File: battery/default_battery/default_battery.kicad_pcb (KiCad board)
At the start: 2 copper layers, 14 parts

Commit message: add battery_led_back
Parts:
- moved BAT_Q1 0.65 mm to (0.00, -41.3)
- moved BAT_AP1 0.37 mm to (0.00, -37.4), turned to -90 degrees
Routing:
- net VBUS: track 28.5 -> 24.9 mm, vias 1 -> 0
- net GND: track 37.8 -> 38.9 mm
- net Net-(BAT_AP1-EN): track 11.0 -> 10.5 mm

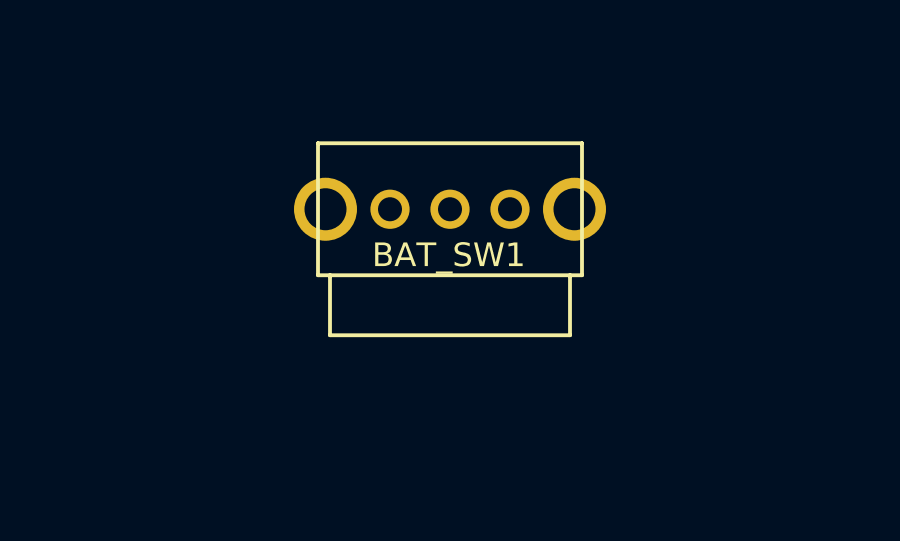
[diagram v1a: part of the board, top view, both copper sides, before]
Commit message: update battery switch symbol
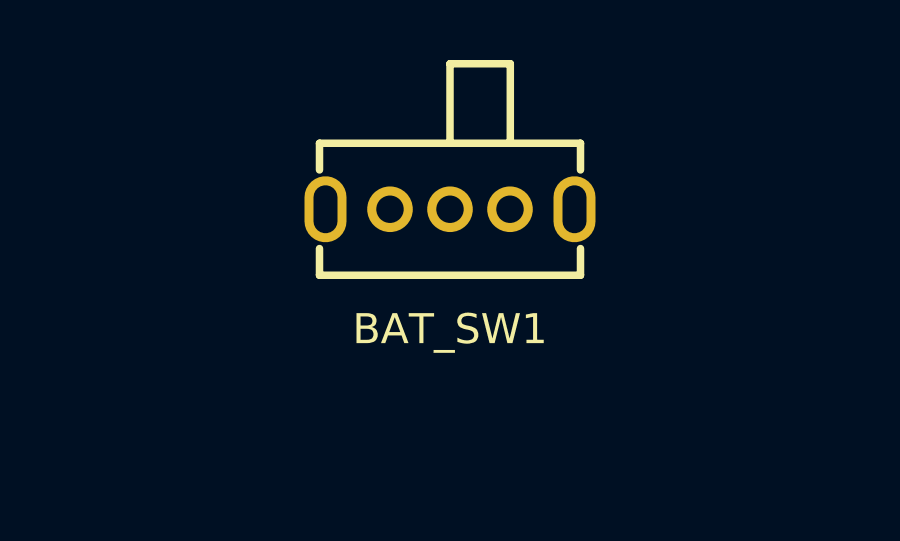
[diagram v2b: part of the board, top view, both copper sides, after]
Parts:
- BAT_SW1: footprint ErgoCai.pretty:SK12D07VG4 -> easyeda2kicad:SW-TH_SK12D07VG4
- turned BAT_SW1 to 180 degrees
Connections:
- BAT_SW1 pad 2: unconnected-(BAT_SW1-Pad2) -> VBAT
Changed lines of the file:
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@@
 	(net 12 "Net-(BAT_TP1-~{CHRG})")
 	(net 13 "Net-(BAT_TP1-PROG)")
-	(net 14 "unconnected-(BAT_SW1-Pad2)")
+	(net 14 "unconnected-(BAT_SW1-Pad3)")
 	(footprint "ErgoCai.pretty:R_0603_1608Metric"
 		(layer "F.Cu")
@@
 			)
 		)
-		(property "Datasheet" ""
+		(property "Datasheet" "~"
 			(at 0 0 0)
 			(unlocked yes)
@@
 			)
 		)
-		(property "Datasheet" ""
+		(property "Datasheet" "~"
 			(at 0 0 180)
 			(unlocked yes)
@@
 			)
 		)
-		(property "Datasheet" ""
+		(property "Datasheet" "~"
 			(at 0 0 180)
 			(unlocked yes)
@@
 			)
 		)
-		(property "Datasheet" ""
+		(property "Datasheet" "~"
 			(at 0 0 180)
 			(unlocked yes)
@@
 			)
 		)
-		(property "Datasheet" ""
+		(property "Datasheet" "~"
 			(at 0 0 180)
 			(unlocked yes)
@@
 			)
 		)
-		(property "Datasheet" ""
+		(property "Datasheet" "~"
 			(at 0 0 180)
 			(unlocked yes)
@@
 			)
 		)
-		(property "Datasheet" ""
+		(property "Datasheet" "~"
 			(at 0 0 0)
 			(unlocked yes)
@@
 		)
 	)
-	(footprint "ErgoCai.pretty:SK12D07VG4"
+	(footprint "easyeda2kicad:SW-TH_SK12D07VG4"
 		(layer "F.Cu")
-		(at -0.49 -58.65)
+		(at -0.49 -58.65 180)
 		(property "Reference" "BAT_SW1"
-			(at -0.04 1.53 0)
-			(layer "F.SilkS")
-			(effects
-				(font
-					(size 0.787402 0.787402)
+			(at 0 -4 0)
+			(layer "F.SilkS")
+			(effects
+				(font
+					(size 1 1)
 					(thickness 0.15)
 				)
@@
 		)
 		(property "Value" "~"
-			(at 0.01 3.18 0)
-			(layer "F.Fab")
-			(effects
-				(font
-					(size 0.787402 0.787402)
-					(thickness 0.15)
-				)
-			)
-		)
-		(property "Datasheet" ""
+			(at 0 4 0)
+			(layer "F.Fab")
+			(effects
+				(font
+					(size 1 1)
+					(thickness 0.15)
+				)
+			)
+		)
+		(property "Datasheet" "https://lcsc.com/product-detail/Toggle-Switches_SHOU-HAN-SK12D07VG4_C393937.html"
 			(at 0 0 0)
 			(layer "F.Fab")
@@
 		)
 		(property "MF" "C&K"
-			(at 0 0 0)
+			(at 0 0 180)
 			(unlocked yes)
 			(layer "F.Fab")
@@
 		)
 		(property "Description_1" "Switch Slide ON ON SPDT Side Slide 0.3A 30VDC PC Pins Bracket Mount/Through Hole Bulk"
-			(at 0 0 0)
+			(at 0 0 180)
 			(unlocked yes)
 			(layer "F.Fab")
@@
 		)
 		(property "Package" "None"
-			(at 0 0 0)
+			(at 0 0 180)
 			(unlocked yes)
 			(layer "F.Fab")
@@
 		)
 		(property "Price" "None"
-			(at 0 0 0)
+			(at 0 0 180)
 			(unlocked yes)
 			(layer "F.Fab")
@@
 		)
 		(property "SnapEDA_Link" "https://www.snapeda.com/parts/SK12D07VG4/C%2526K/view-part/?ref=snap"
-			(at 0 0 0)
+			(at 0 0 180)
 			(unlocked yes)
 			(layer "F.Fab")
@@
 		)
 		(property "MP" "SK12D07VG4"
-			(at 0 0 0)
+			(at 0 0 180)
 			(unlocked yes)
 			(layer "F.Fab")
@@
 		)
 		(property "Availability" "Not in stock"
-			(at 0 0 0)
+			(at 0 0 180)
 			(unlocked yes)
 			(layer "F.Fab")
@@
 		)
 		(property "Check_prices" "https://www.snapeda.com/parts/SK12D07VG4/C%2526K/view-part/?ref=eda"
-			(at 0 0 0)
+			(at 0 0 180)
+			(unlocked yes)
+			(layer "F.Fab")
+			(hide yes)
+			(effects
+				(font
+					(size 1 1)
+					(thickness 0.15)
+				)
+			)
+		)
+		(property "LCSC Part" "C393937"
+			(at 0 0 180)
 			(unlocked yes)
 			(layer "F.Fab")
@@
 		(attr through_hole)
 		(fp_line
-			(start -4.4 -2.2)
-			(end 4.4 -2.2)
-			(stroke
-				(width 0.127)
-				(type solid)
-			)
-			(layer "F.SilkS")
-		)
-		(fp_line
-			(start -4.4 2.2)
-			(end -4.4 -2.2)
-			(stroke
-				(width 0.127)
-				(type solid)
-			)
-			(layer "F.SilkS")
-		)
-		(fp_line
-			(start -4 2.2)
-			(end -4.4 2.2)
-			(stroke
-				(width 0.127)
-				(type solid)
-			)
-			(layer "F.SilkS")
-		)
-		(fp_line
-			(start -4 2.2)
-			(end -4 4.2)
-			(stroke
-				(width 0.127)
-				(type solid)
-			)
-			(layer "F.SilkS")
-		)
-		(fp_line
-			(start -4 4.2)
-			(end 4 4.2)
-			(stroke
-				(width 0.127)
-				(type solid)
-			)
-			(layer "F.SilkS")
-		)
-		(fp_line
-			(start 4 2.2)
-			(end -4 2.2)
-			(stroke
-				(width 0.127)
-				(type solid)
-			)
-			(layer "F.SilkS")
-		)
-		(fp_line
-			(start 4 4.2)
-			(end 4 2.2)
-			(stroke
-				(width 0.127)
-				(type solid)
-			)
-			(layer "F.SilkS")
-		)
-		(fp_line
-			(start 4.4 -2.2)
-			(end 4.4 2.2)
-			(stroke
-				(width 0.127)
-				(type solid)
-			)
-			(layer "F.SilkS")
-		)
-		(fp_line
-			(start 4.4 2.2)
-			(end 4 2.2)
-			(stroke
-				(width 0.127)
-				(type solid)
-			)
-			(layer "F.SilkS")
+			(start 4.35 2.2)
+			(end -4.35 2.2)
+			(stroke
+				(width 0.25)
+				(type solid)
+			)
+			(layer "F.SilkS")
+		)
+		(fp_line
+			(start 4.35 1.31)
+			(end 4.35 2.2)
+			(stroke
+				(width 0.25)
+				(type solid)
+			)
+			(layer "F.SilkS")
+		)
+		(fp_line
+			(start 4.35 -2.2)
+			(end 4.35 -1.31)
+			(stroke
+				(width 0.25)
+				(type solid)
+			)
+			(layer "F.SilkS")
+		)
+		(fp_line
+			(start 0 4.85)
+			(end 0 2.2)
+			(stroke
+				(width 0.25)
+				(type solid)
+			)
+			(layer "F.SilkS")
+		)
+		(fp_line
+			(start -2.01 4.85)
+			(end 0 4.85)
+			(stroke
+				(width 0.25)
+				(type solid)
+			)
+			(layer "F.SilkS")
+		)
+		(fp_line
+			(start -2.01 2.2)
+			(end -2.01 4.85)
+			(stroke
+				(width 0.25)
+				(type solid)
+			)
+			(layer "F.SilkS")
+		)
+		(fp_line
+			(start -4.35 2.2)
+			(end -4.35 1.31)
+			(stroke
+				(width 0.25)
+				(type solid)
+			)
+			(layer "F.SilkS")
+		)
+		(fp_line
+			(start -4.35 -1.31)
+			(end -4.35 -2.2)
+			(stroke
+				(width 0.25)
+				(type solid)
+			)
+			(layer "F.SilkS")
+		)
+		(fp_line
+			(start -4.35 -2.2)
+			(end 4.35 -2.2)
+			(stroke
+				(width 0.25)
+				(type solid)
+			)
+			(layer "F.SilkS")
+		)
+		(fp_circle
+			(center -4.47 2.2)
+			(end -4.44 2.2)
+			(stroke
+				(width 0.06)
+				(type solid)
+			)
+			(fill no)
+			(layer "F.Fab")
+		)
+		(fp_text user "${REFERENCE}"
+			(at 0 0 0)
+			(layer "F.Fab")
+			(effects
+				(font
+					(size 1 1)
+					(thickness 0.15)
+				)
+			)
 		)
 		(pad "1" thru_hole circle
-			(at -2 0)
-			(size 1.308 1.308)
-			(drill 0.8)
+			(at -2 0 180)
+			(size 1.52 1.52)
+			(drill 0.9144)
 			(layers "*.Cu" "*.Mask")
 			(remove_unused_layers no)
 			(net 5 "Net-(BAT_Q1-D)")
 			(pinfunction "1")
-			(pintype "bidirectional")
-			(solder_mask_margin 0.102)
+			(pintype "unspecified")
 		)
 		(pad "2" thru_hole circle
-			(at 2 0)
-			(size 1.308 1.308)
-			(drill 0.8)
-			(layers "*.Cu" "*.Mask")
-			(remove_unused_layers no)
-			(net 14 "unconnected-(BAT_SW1-Pad2)")
-			(pinfunction "2")
-			(pintype "bidirectional+no_connect")
-			(solder_mask_margin 0.102)
-		)
-		(pad "COM" thru_hole circle
-			(at 0 0)
-			(size 1.308 1.308)
-			(drill 0.8)
+			(at 0 0 180)
+			(size 1.52 1.52)
+			(drill 0.9144)
 			(layers "*.Cu" "*.Mask")
 			(remove_unused_layers no)
 			(net 1 "VBAT")
-			(pinfunction "COM")
-			(pintype "bidirectional")
-			(solder_mask_margin 0.102)
-		)
-		(pad "M1" thru_hole circle
-			(at -4.15 0)
-			(size 2.1 2.1)
-			(drill 1.4)
+			(pinfunction "2")
+			(pintype "unspecified")
+		)
+		(pad "3" thru_hole circle
+			(at 2 0 180)
+			(size 1.52 1.52)
+			(drill 0.9144)
 			(layers "*.Cu" "*.Mask")
 			(remove_unused_layers no)
-			(solder_mask_margin 0.102)
-		)
-		(pad "M2" thru_hole circle
-			(at 4.15 0)
-			(size 2.1 2.1)
-			(drill 1.4)
+			(net 14 "unconnected-(BAT_SW1-Pad3)")
+			(pinfunction "3")
+			(pintype "unspecified+no_connect")
+		)
+		(pad "4" thru_hole oval
+			(at 4.15 0 180)
+			(size 1.4 2.2)
+			(drill oval 0.799998 1.599997)
 			(layers "*.Cu" "*.Mask")
 			(remove_unused_layers no)
-			(solder_mask_margin 0.102)
+			(net 2 "GND")
+			(pinfunction "4")
+			(pintype "unspecified")
+		)
+		(pad "5" thru_hole oval
+			(at -4.15 0 180)
+			(size 1.4 2.2)
+			(drill oval 0.799998 1.599997)
+			(layers "*.Cu" "*.Mask")
+			(remove_unused_layers no)
+			(net 2 "GND")
+			(pinfunction "5")
+			(pintype "unspecified")
 		)
 		(embedded_fonts no)
-		(model "/Users/jinsongc/Development/ErgoCaiLib/3dmodels/SK12D07VG4.step"
+		(model "${EASYEDA2KICAD}/easyeda2kicad.3dshapes/SW-TH_L8.7-W4.4-H4.0-P2.0.wrl"
 			(offset
-				(xyz 0 0 0)
+				(xyz 0 -1.3 0)
 			)
 			(scale
@@
 			)
 			(rotate
-				(xyz 90 -180 -0)
+				(xyz 0 0 0)
 			)
 		)
@@
 			)
 		)
-		(property "Datasheet" ""
+		(property "Datasheet" "~"
 			(at 0 0 0)
 			(unlocked yes)
@@
 			)
 		)
-		(property "Datasheet" ""
+		(property "Datasheet" "~"
 			(at 0 0 0)
 			(layer "F.Fab")
@@
 			)
 		)
-		(property "Datasheet" ""
+		(property "Datasheet" "~"
 			(at 0 0 0)
 			(unlocked yes)
